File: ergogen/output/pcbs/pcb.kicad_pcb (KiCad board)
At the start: 2 copper layers, 134 x 87 mm, 32 parts

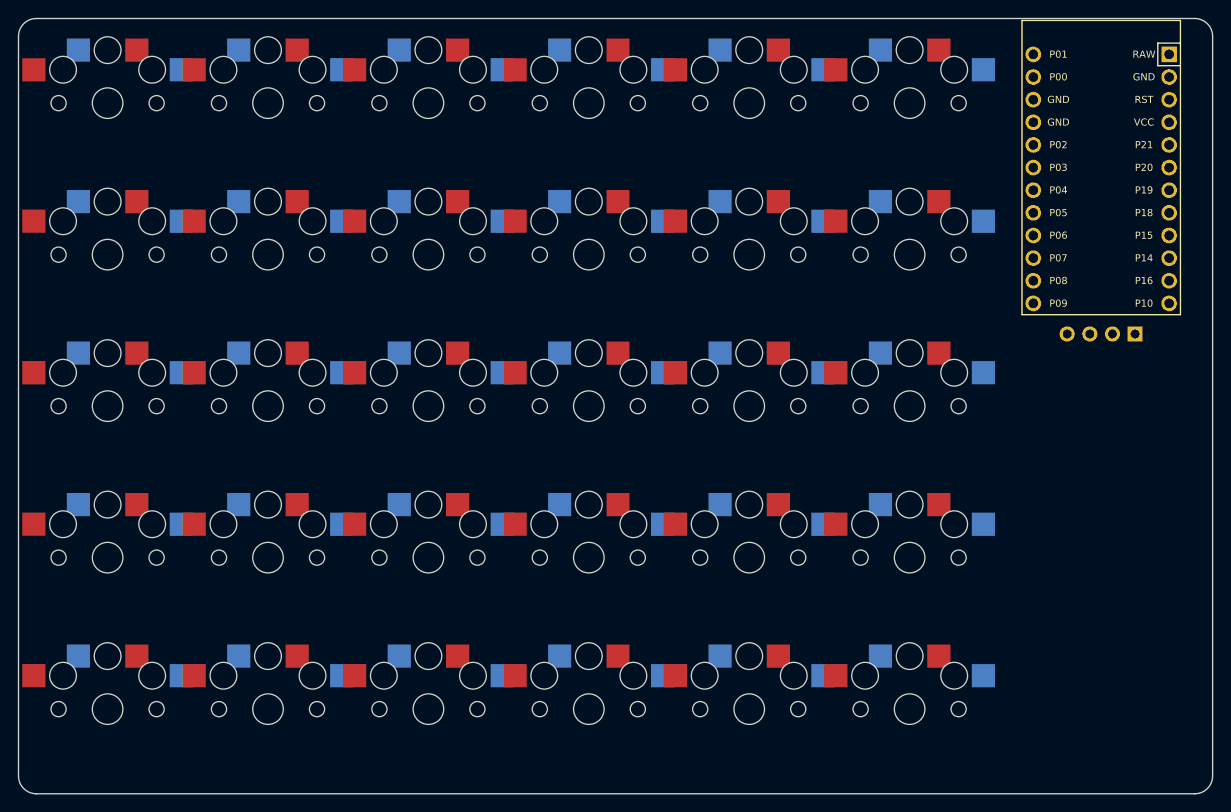
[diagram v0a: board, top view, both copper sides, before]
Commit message: Changed the footprints.
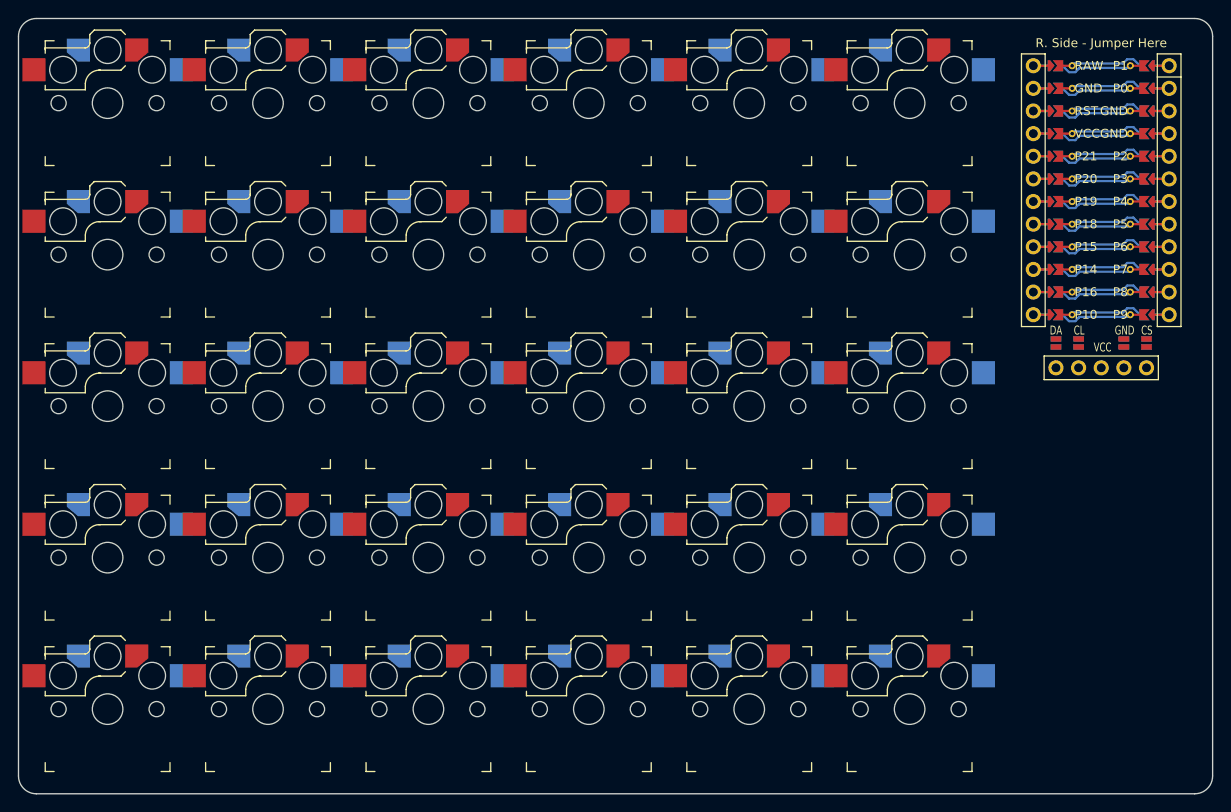
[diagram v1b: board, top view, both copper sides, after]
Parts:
- removed OLED1: OLED, lib:OLED_headers
- added DISP1: , nice!view, F.Cu at (156.5, 45.0)
- MCU1: footprint ProMicro -> nice_nano
- turned MCU1 to 0 degrees
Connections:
- net P10 renamed MCU1_12
- net P14 renamed MCU1_10
- net P15 renamed MCU1_9
- net P16 renamed MCU1_11
- net P18 renamed MCU1_8
- net P19 renamed MCU1_7
- net P20 renamed MCU1_6
- net P21 renamed MCU1_5
- net RAW renamed MCU1_1
- net RST renamed MCU1_3
- MCU1 pad 13: P1 -> MCU1_13
- MCU1 pad 14: P0 -> MCU1_14
- MCU1 pad 15: GND -> MCU1_15
- MCU1 pad 16: GND -> MCU1_16
- MCU1 pad 17: P2 -> MCU1_17
- MCU1 pad 18: P3 -> MCU1_18
- MCU1 pad 19: P4 -> MCU1_19
- MCU1 pad 2: GND -> MCU1_2
- MCU1 pad 20: P5 -> MCU1_20
- MCU1 pad 21: P6 -> MCU1_21
- MCU1 pad 22: P7 -> MCU1_22
- MCU1 pad 23: P8 -> MCU1_23
- MCU1 pad 24: P9 -> MCU1_24
- MCU1 pad 4: VCC -> MCU1_4
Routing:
- net outer_mod: track 0.00 -> 122.1 mm
- net ring_home: track 0.00 -> 122.0 mm
- net index_top: track 0.00 -> 50.9 mm
- net index_home: track 0.00 -> 50.9 mm

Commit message: Added components.
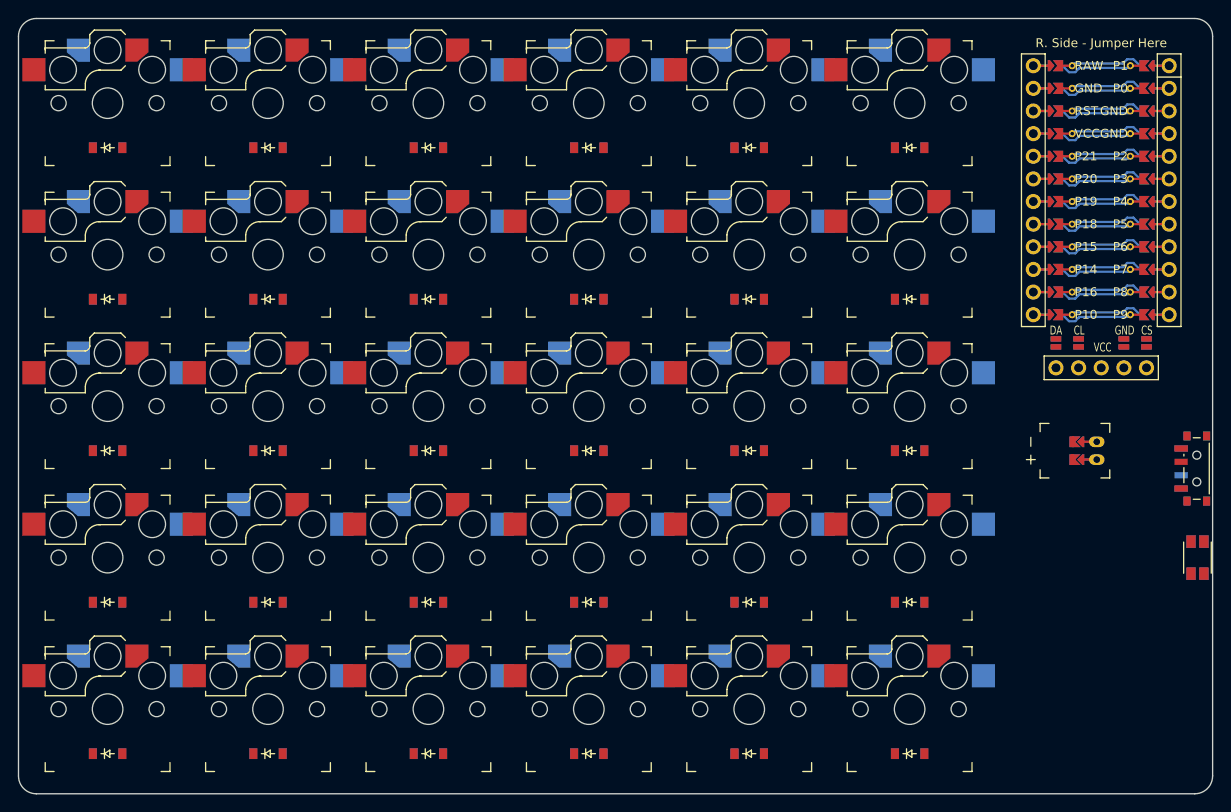
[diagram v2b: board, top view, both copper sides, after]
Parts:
- added D1: , ComboDiode, F.Cu at (45.0, 105.0)
- added D10: , ComboDiode, F.Cu at (63.0, 37.0)
- added D11: , ComboDiode, F.Cu at (81.0, 105.0)
- added D12: , ComboDiode, F.Cu at (81.0, 88.0)
- added D13: , ComboDiode, F.Cu at (81.0, 71.0)
- added D14: , ComboDiode, F.Cu at (81.0, 54.0)
- added D15: , ComboDiode, F.Cu at (81.0, 37.0)
- added D16: , ComboDiode, F.Cu at (99.0, 105.0)
- added D17: , ComboDiode, F.Cu at (99.0, 88.0)
- added D18: , ComboDiode, F.Cu at (99.0, 71.0)
- added D19: , ComboDiode, F.Cu at (99.0, 54.0)
- added D2: , ComboDiode, F.Cu at (45.0, 88.0)
- added D20: , ComboDiode, F.Cu at (99.0, 37.0)
- added D21: , ComboDiode, F.Cu at (117.0, 105.0)
- added D22: , ComboDiode, F.Cu at (117.0, 88.0)
- added D23: , ComboDiode, F.Cu at (117.0, 71.0)
- added D24: , ComboDiode, F.Cu at (117.0, 54.0)
- added D25: , ComboDiode, F.Cu at (117.0, 37.0)
- added D26: , ComboDiode, F.Cu at (135.0, 105.0)
- added D27: , ComboDiode, F.Cu at (135.0, 88.0)
- added D28: , ComboDiode, F.Cu at (135.0, 71.0)
- added D29: , ComboDiode, F.Cu at (135.0, 54.0)
- added D3: , ComboDiode, F.Cu at (45.0, 71.0)
- added D30: , ComboDiode, F.Cu at (135.0, 37.0)
- added D4: , ComboDiode, F.Cu at (45.0, 54.0)
- added D5: , ComboDiode, F.Cu at (45.0, 37.0)
- added D6: , ComboDiode, F.Cu at (63.0, 105.0)
- added D7: , ComboDiode, F.Cu at (63.0, 88.0)
- added D8: , ComboDiode, F.Cu at (63.0, 71.0)
- added D9: , ComboDiode, F.Cu at (63.0, 54.0)
- added JST1: , ceoloide:battery_connector_jst_ph_2, F.Cu at (156.0, 71.0)
- added SW1: , sw_reset_side, F.Cu at (167.3, 83.0)
- added SW2: , power_switch, F.Cu at (167.2, 73.0)
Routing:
- net JST1_2: track 0.00 -> 3.60 mm
- net JST1_1: track 0.00 -> 3.60 mm
